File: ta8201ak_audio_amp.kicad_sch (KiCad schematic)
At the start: 20 parts, among them J1 IN, J2 Out1, J3 Vcc, J4 Gnd, J5 Out2

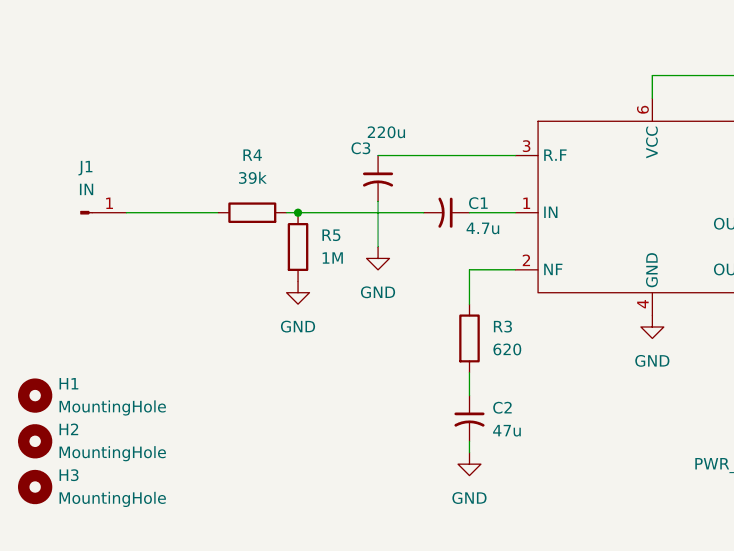
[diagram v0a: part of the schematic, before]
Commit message: エレキギター向けに抵抗やコンデンサを変更
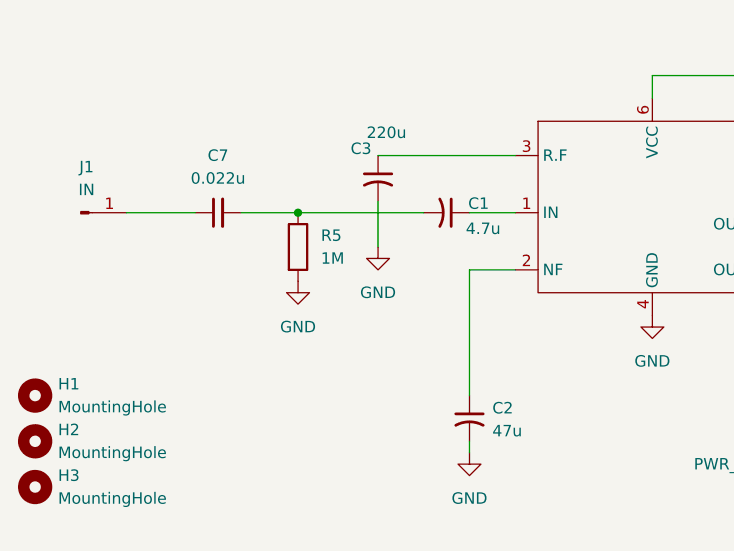
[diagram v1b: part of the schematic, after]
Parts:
- removed R3: 620, Resistor_THT:R_Axial_DIN0411_L9.9mm_D3.6mm_P5.08mm_Vertical, symbol Device:R
- removed R4: 39k, Resistor_THT:R_Axial_DIN0411_L9.9mm_D3.6mm_P5.08mm_Vertical, symbol Device:R
- added C7: 0.022u, Capacitor_THT:C_Rect_L7.0mm_W2.5mm_P5.00mm, symbol Device:C_Small
- R5: footprint Resistor_THT:R_Axial_DIN0411_L9.9mm_D3.6mm_P5.08mm_Vertical -> Resistor_THT:R_Axial_DIN0207_L6.3mm_D2.5mm_P5.08mm_Vertical
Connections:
- net at J1.1 (Pin_1): now also C7.1
- net at U1.2 (NF): now also C2.1
- net at C1.2, R5.1: now also C7.2
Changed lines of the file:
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@@
-	(wire
-		(pts
-			(xy 115.57 101.6) (xy 116.84 101.6)
-		)
-		(stroke
-			(width 0)
-			(type default)
-		)
-	)
 	(wire
 		(pts
@@
 	(wire
 		(pts
-			(xy 97.79 101.6) (xy 107.95 101.6)
+			(xy 97.79 101.6) (xy 105.41 101.6)
 		)
 		(stroke
@@
 	(wire
 		(pts
-			(xy 135.89 119.38) (xy 135.89 121.92)
+			(xy 135.89 107.95) (xy 135.89 121.92)
 		)
 		(stroke
@@
 	(wire
 		(pts
-			(xy 135.89 107.95) (xy 135.89 111.76)
-		)
-		(stroke
-			(width 0)
-			(type default)
-		)
-	)
-	(wire
-		(pts
 			(xy 185.42 115.57) (xy 185.42 121.92)
 		)
@@
 		(pts
 			(xy 116.84 101.6) (xy 130.81 101.6)
+		)
+		(stroke
+			(width 0)
+			(type default)
+		)
+	)
+	(wire
+		(pts
+			(xy 110.49 101.6) (xy 116.84 101.6)
 		)
 		(stroke
@@
 				(path "/3e27d207-50b8-40b2-b752-3d08c7aa128e"
 					(reference "J1")
+					(unit 1)
+				)
+			)
+		)
+	)
+	(symbol
+		(lib_id "Device:C_Small")
+		(at 107.95 101.6 90)
+		(unit 1)
+		(exclude_from_sim no)
+		(in_bom yes)
+		(on_board yes)
+		(dnp no)
+		(fields_autoplaced yes)
+		(property "Reference" "C7"
+			(at 107.9563 95.25 90)
+			(effects
+				(font
+					(size 1.27 1.27)
+				)
+			)
+		)
+		(property "Value" "0.022u"
+			(at 107.9563 97.79 90)
+			(effects
+				(font
+					(size 1.27 1.27)
+				)
+			)
+		)
+		(property "Footprint" "Capacitor_THT:C_Rect_L7.0mm_W2.5mm_P5.00mm"
+			(at 107.95 101.6 0)
+			(effects
+				(font
+					(size 1.27 1.27)
+				)
+				(hide yes)
+			)
+		)
+		(property "Datasheet" "~"
+			(at 107.95 101.6 0)
+			(effects
+				(font
+					(size 1.27 1.27)
+				)
+				(hide yes)
+			)
+		)
+		(property "Description" "Unpolarized capacitor, small symbol"
+			(at 107.95 101.6 0)
+			(effects
+				(font
+					(size 1.27 1.27)
+				)
+				(hide yes)
+			)
+		)
+		(pin "2"
+		)
+		(pin "1"
+		)
+		(instances
+			(project "ta8201ak_audio_amp"
+				(path "/3e27d207-50b8-40b2-b752-3d08c7aa128e"
+					(reference "C7")
 					(unit 1)
 				)
@@
 	)
 	(symbol
-		(lib_id "Device:R")
-		(at 135.89 115.57 0)
-		(unit 1)
-		(exclude_from_sim no)
-		(in_bom yes)
-		(on_board yes)
-		(dnp no)
-		(fields_autoplaced yes)
-		(property "Reference" "R3"
-			(at 138.43 114.2999 0)
-			(effects
-				(font
-					(size 1.27 1.27)
-				)
-				(justify left)
-			)
-		)
-		(property "Value" "620"
-			(at 138.43 116.8399 0)
-			(effects
-				(font
-					(size 1.27 1.27)
-				)
-				(justify left)
-			)
-		)
-		(property "Footprint" "Resistor_THT:R_Axial_DIN0411_L9.9mm_D3.6mm_P5.08mm_Vertical"
-			(at 134.112 115.57 90)
-			(effects
-				(font
-					(size 1.27 1.27)
-				)
-				(hide yes)
-			)
-		)
-		(property "Datasheet" "~"
-			(at 135.89 115.57 0)
-			(effects
-				(font
-					(size 1.27 1.27)
-				)
-				(hide yes)
-			)
-		)
-		(property "Description" "Resistor"
-			(at 135.89 115.57 0)
-			(effects
-				(font
-					(size 1.27 1.27)
-				)
-				(hide yes)
-			)
-		)
-		(pin "1"
-		)
-		(pin "2"
-		)
-		(instances
-			(project "ta8201ak_audio_amp"
-				(path "/3e27d207-50b8-40b2-b752-3d08c7aa128e"
-					(reference "R3")
-					(unit 1)
-				)
-			)
-		)
-	)
-	(symbol
-		(lib_id "Device:R")
-		(at 111.76 101.6 90)
-		(unit 1)
-		(exclude_from_sim no)
-		(in_bom yes)
-		(on_board yes)
-		(dnp no)
-		(fields_autoplaced yes)
-		(property "Reference" "R4"
-			(at 111.76 95.25 90)
-			(effects
-				(font
-					(size 1.27 1.27)
-				)
-			)
-		)
-		(property "Value" "39k"
-			(at 111.76 97.79 90)
-			(effects
-				(font
-					(size 1.27 1.27)
-				)
-			)
-		)
-		(property "Footprint" "Resistor_THT:R_Axial_DIN0411_L9.9mm_D3.6mm_P5.08mm_Vertical"
-			(at 111.76 103.378 90)
-			(effects
-				(font
-					(size 1.27 1.27)
-				)
-				(hide yes)
-			)
-		)
-		(property "Datasheet" "~"
-			(at 111.76 101.6 0)
-			(effects
-				(font
-					(size 1.27 1.27)
-				)
-				(hide yes)
-			)
-		)
-		(property "Description" "Resistor"
-			(at 111.76 101.6 0)
-			(effects
-				(font
-					(size 1.27 1.27)
-				)
-				(hide yes)
-			)
-		)
-		(pin "1"
-		)
-		(pin "2"
-		)
-		(instances
-			(project "ta8201ak_audio_amp"
-				(path "/3e27d207-50b8-40b2-b752-3d08c7aa128e"
-					(reference "R4")
-					(unit 1)
-				)
-			)
-		)
-	)
-	(symbol
 		(lib_id "power:GND")
 		(at 125.73 105.41 0)
@@
 			)
 		)
-		(property "Footprint" "Resistor_THT:R_Axial_DIN0411_L9.9mm_D3.6mm_P5.08mm_Vertical"
+		(property "Footprint" "Resistor_THT:R_Axial_DIN0207_L6.3mm_D2.5mm_P5.08mm_Vertical"
 			(at 115.062 105.41 90)
 			(effects

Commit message: 利得制限の抵抗は外した アッテネーターの合成抵抗をエレキギター向けに1Mに近づけた 高音補正用のセラミックコンデンサとボリュームを追加
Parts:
- added J2: RV1_3, Connector_PinHeader_2.54mm:PinHeader_1x01_P2.54mm_Vertical, symbol Connector:Conn_01x01_Pin
- added J3: RV1_2, Connector_PinHeader_2.54mm:PinHeader_1x01_P2.54mm_Vertical, symbol Connector:Conn_01x01_Pin
- added J8: SW1_1, Connector_PinHeader_2.54mm:PinHeader_1x01_P2.54mm_Vertical, symbol Connector:Conn_01x01_Pin
- added J9: SW1_2, Connector_PinHeader_2.54mm:PinHeader_1x01_P2.54mm_Vertical, symbol Connector:Conn_01x01_Pin
- added R1: 200k, Resistor_THT:R_Axial_DIN0207_L6.3mm_D2.5mm_P2.54mm_Vertical, symbol Device:R
- added RV1: 1m, symbol Device:R_Potentiometer
- added SW1: Hi, symbol Switch:SW_SPST
- C7: value 0.022u -> 100p; footprint Capacitor_THT:C_Rect_L7.0mm_W2.5mm_P5.00mm -> Capacitor_THT:C_Disc_D5.0mm_W2.5mm_P2.50mm
- R2: renamed from R5; value 1M -> 820k; footprint Resistor_THT:R_Axial_DIN0207_L6.3mm_D2.5mm_P5.08mm_Vertical -> Resistor_THT:R_Axial_DIN0207_L6.3mm_D2.5mm_P2.54mm_Vertical
- renumbered C3 to C1, C1 to C2, C2 to C3, C5 to C4, C4 to C5, J2 to J4, J3 to J6, J4 to J7, R1 to R3, R2 to R4
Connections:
- net GND: now also RV1.1
- net at J1.1 (Pin_1): now also J8.1 (Pin_1), R1.1, SW1.1 (A); no longer C7.1
- net at C7.2, R2.1: now also J2.1 (Pin_1), R1.2, RV1.3; no longer C2.2
- new net: C2.2, J3.1 (Pin_1), RV1.2
- new net: C7.1, J9.1 (Pin_1), SW1.2 (B)
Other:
- moved on the sheet: C3, J1, R2

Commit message: ベタGNDをやめ、音声がICに入るまでのGNDと電源のGNDを分離した。
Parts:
- removed J7: Gnd, Connector_PinHeader_2.54mm:PinHeader_1x01_P2.54mm_Vertical, symbol Connector:Conn_01x01_Pin
- added J1: AudioJack3, symbol Connector_Audio:AudioJack3
- added J3: Gnd, Connector_PinHeader_2.54mm:PinHeader_1x01_P2.54mm_Vertical, symbol Connector:Conn_01x01_Pin
- added J4: AudioGnd, Connector_PinHeader_2.54mm:PinHeader_1x01_P2.54mm_Vertical, symbol Connector:Conn_01x01_Pin
- renumbered C7 to C1, C5 to C2, C1 to C3, C2 to C4, C3 to C5, C4 to C6, C6 to C7, J3 to J10, J4 to J11, J5 to J12, J1 to J2, J9 to J5, J8 to J6, J6 to J7, J2 to J8
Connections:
- net GND: now also J3.1 (Pin_1); no longer R2.2, RV1.1
- net at J2.1 (Pin_1), J6.1 (Pin_1), R1.1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: now also J1.T
- new net GND2: J1.R, J1.S, J4.1 (Pin_1), R2.2, RV1.1
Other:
- moved on the sheet: C2, J2, J7

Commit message: ブライトスイッチのコンデンサはスイッチ直付けにして配置変更
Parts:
- removed J5: SW1_2, Connector_PinHeader_2.54mm:PinHeader_1x01_P2.54mm_Vertical, symbol Connector:Conn_01x01_Pin
- removed J6: SW1_1, Connector_PinHeader_2.54mm:PinHeader_1x01_P2.54mm_Vertical, symbol Connector:Conn_01x01_Pin
- removed SW1: Hi, symbol Switch:SW_SPST
- added C1: 1n, symbol Device:C_Small
- added SW2: SW_Rotary_1x3_MP, symbol Switch:SW_Rotary_1x3_MP
- C2: renamed from C1; value 100p -> 470p; footprint Capacitor_THT:C_Disc_D5.0mm_W2.5mm_P2.50mm -> (none)
- renumbered C2 to C3, C3 to C4, C4 to C5, C5 to C6, C6 to C7, C7 to C8, J4 to J3, J7 to J4, J8 to J5, J10 to J6, J3 to J7, J11 to J8, J12 to J9
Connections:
- net at C5.2, J6.1 (Pin_1), RV1.2: now also SW2.4
- net at C2.2, J5.1 (Pin_1), R1.2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: now also C1.2
- net at C2.1: now also SW2.2
- new net: C1.1, SW2.3
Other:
- moved on the sheet: C2, C3, J4, J5, J6, J7, R1, R2, RV1

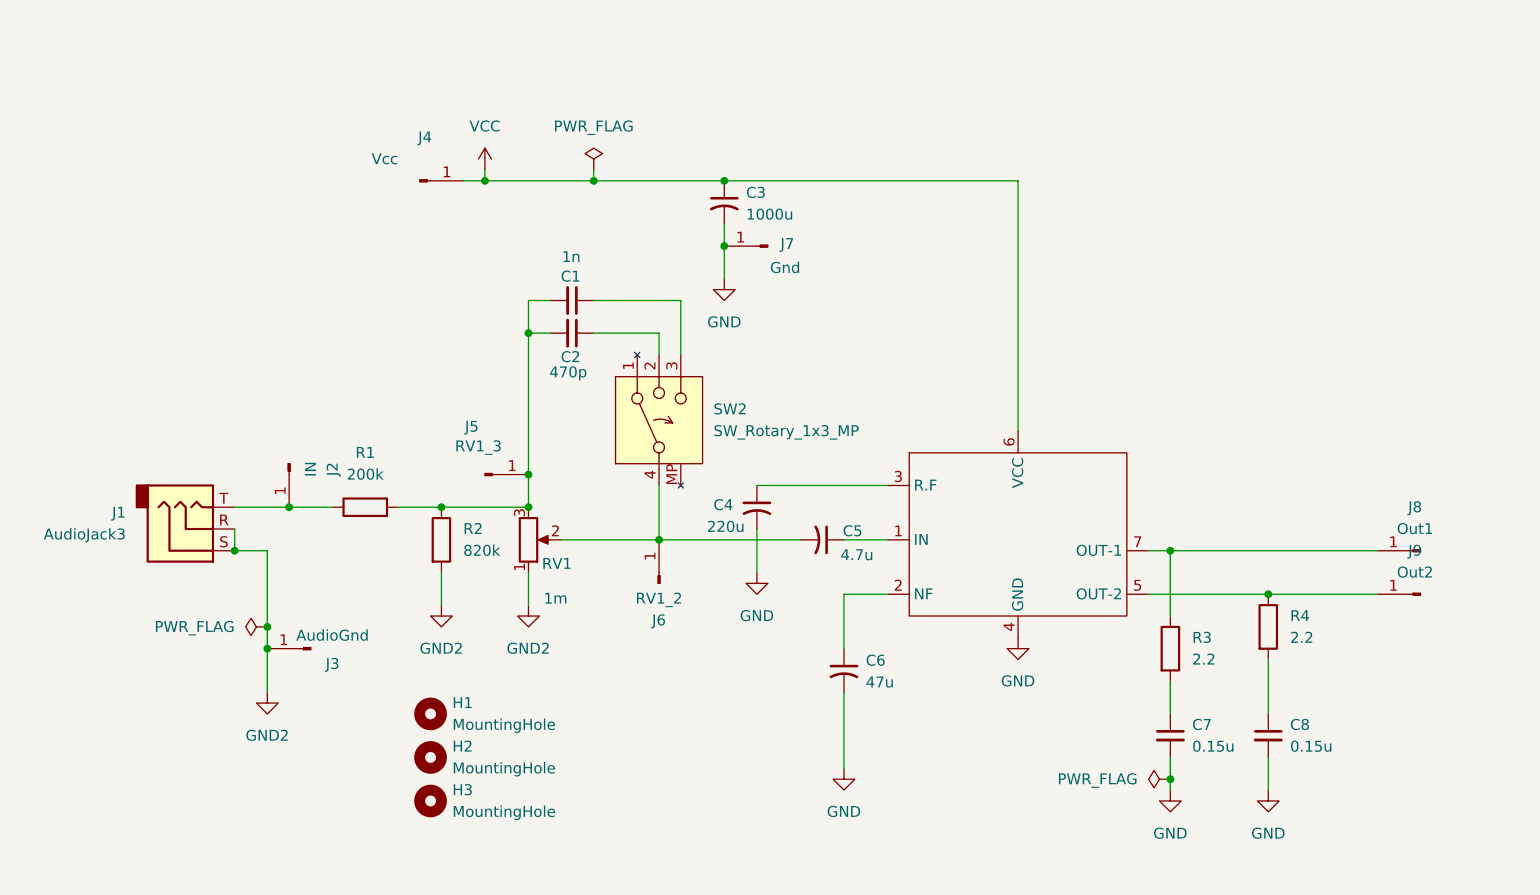
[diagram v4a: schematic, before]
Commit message: ハムノイズ対策に抵抗を追加してGNDの取り方を変更
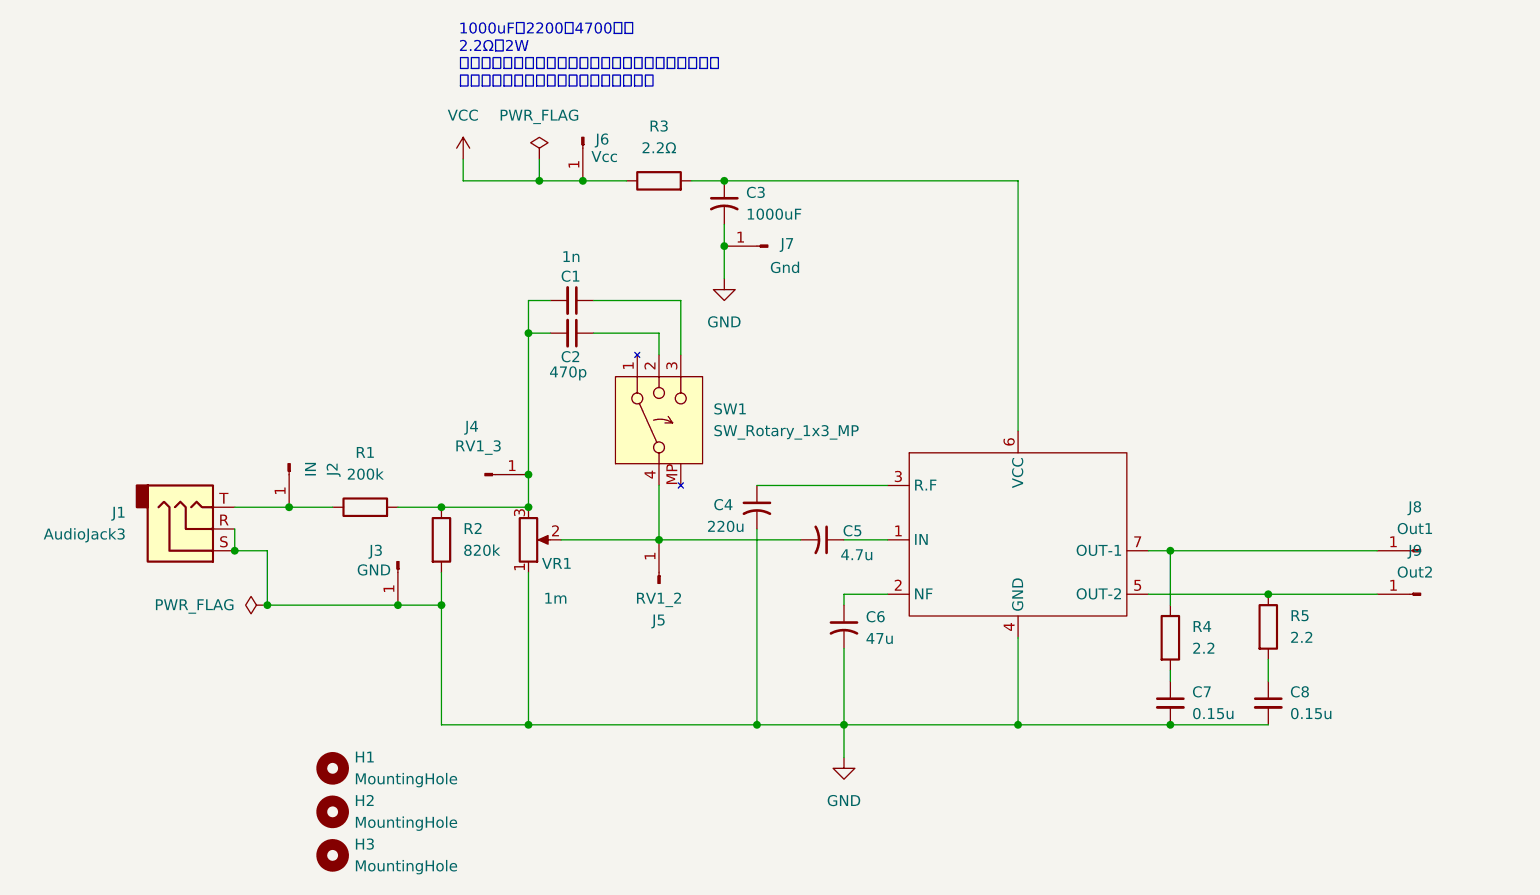
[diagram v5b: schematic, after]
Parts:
- added R3: 2.2Ω, Resistor_THT:R_Axial_DIN0414_L11.9mm_D4.5mm_P5.08mm_Vertical, symbol Device:R
- C3: value 1000u -> 1000uF
- J3: value AudioGnd -> GND
- renumbered J5 to J4, J6 to J5, J4 to J6, R3 to R4, R4 to R5, SW2 to SW1, RV1 to VR1
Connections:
- net GND2 is gone; now on net GND: J1.R, J1.S, J3.1 (Pin_1), R2.2, VR1.1
- net VCC: now also R3.1; no longer C3.1, U1.6 (VCC)
- new net: C3.1, R3.2, U1.6 (VCC)
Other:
- note added: "1000uFは2200や4700推奨 2.2Ωは2W 音声の網線はジャック側は繋がずシールドとして繋ぎ 電源の電解コンデンサのマイナスに繋ぐ"
- moved on the sheet: C6, C7, C8, H1, H2, H3, J6, R4
